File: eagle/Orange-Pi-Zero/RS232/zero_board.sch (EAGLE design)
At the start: 17 parts, among them J1 RS-232, U1 MAX3232CDR

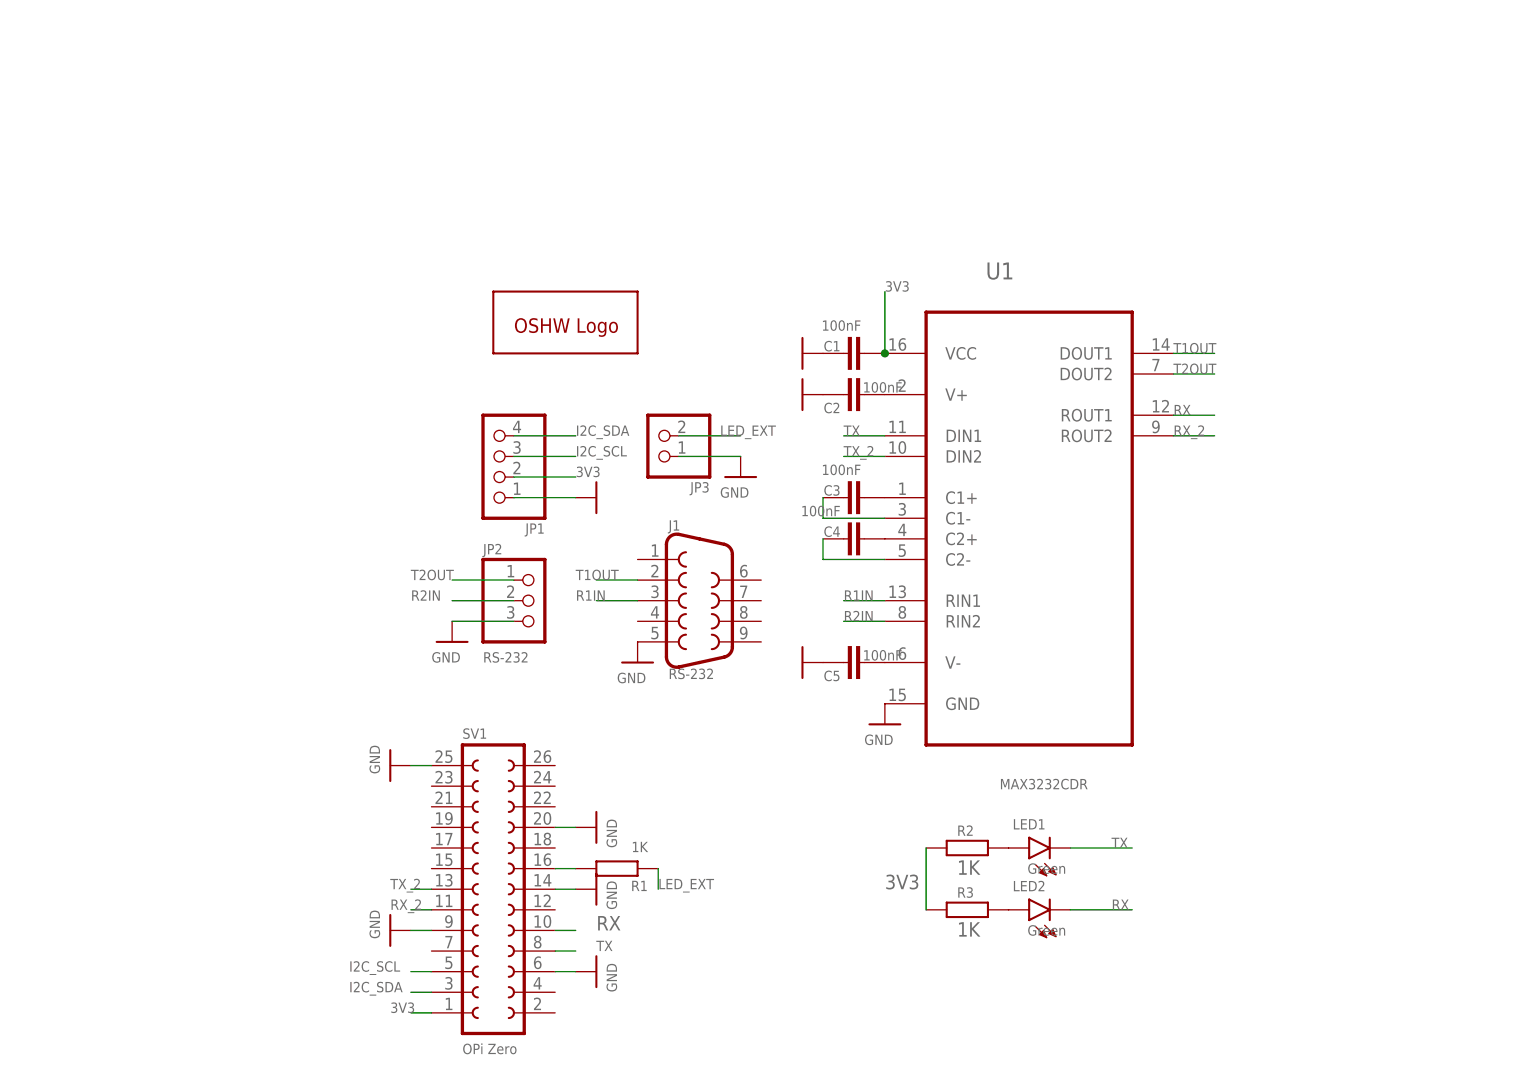
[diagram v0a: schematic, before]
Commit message: Added RGB Panel board.
*. Updated RS232 board
*. Minor fix in BOM fort the 8x pixel board
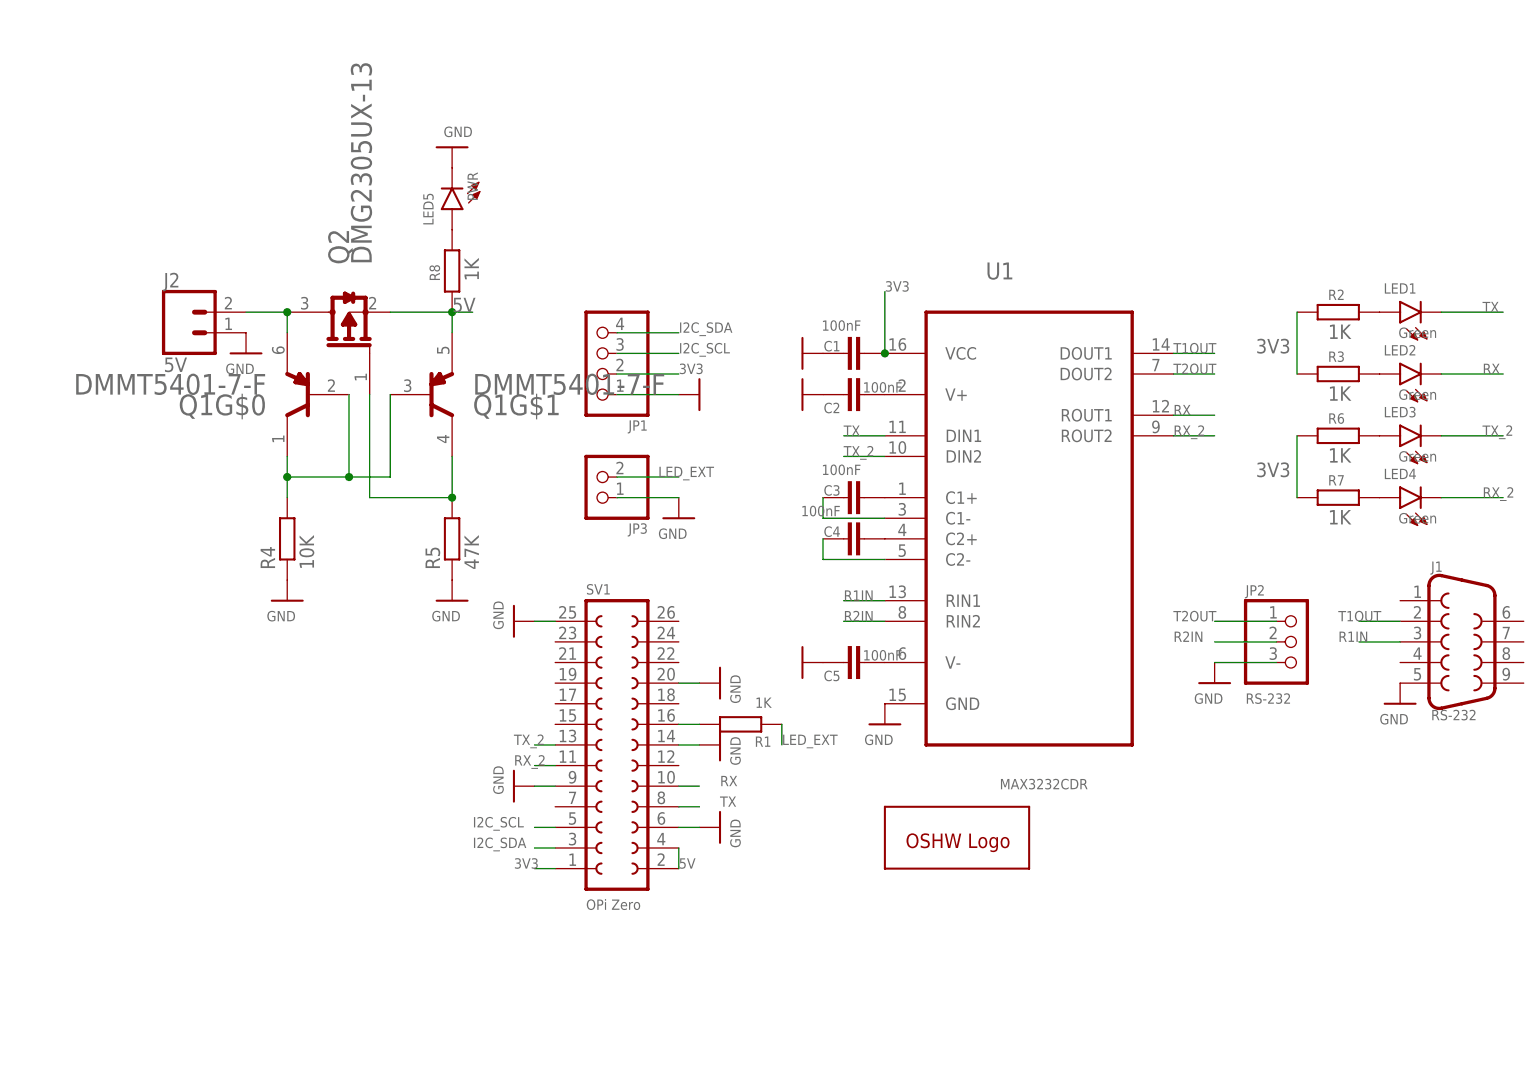
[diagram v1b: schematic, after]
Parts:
- added J2: 5V, SparkFun-Connectors:CONN_023.5MM
- added LED3, LED4: Green, led:LEDCHIP-LED0603
- added LED5: PWR, led:LEDCHIP-LED0603
- added Q1: DIODES_DMMT5401-7-FDIODES_DMMT5401-7-F_0_0, Diodes - DMMT5401-7-F:DIODES_DMMT5401-7-FDIODES_DMMT5401-7-F_0_0
- added Q2: DIODES_INC._DMG2305UX-13DIODES_INC._DMG2305UX-13_0_0, Diodes Inc. - DMG2305UX-13:DIODES_INC._DMG2305UX-13DIODES_INC._DMG2305UX-13_0_0
- added R4: 10K, rcl:R-EU_R0402
- added R5: 47K, rcl:R-EU_R0402
- added R6, R7, R8: 1K, resistor:R-EU_R0603
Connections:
- new net 5V: Q1G$1.E2, Q2.S, R8.1, SV1.2, SV1.4
- new net N$10: Q1G$0.B1, Q1G$0.C1, Q1G$1.B2, R4.2
- new net N$11: J2.2, Q1G$0.E1, Q2.D
- new net N$12: Q1G$1.C2, Q2.G, R5.2
- new net N$13: LED3.A, R6.2
- new net N$14: LED4.A, R7.2
- new net N$15: LED5.A, R8.2
- net 3V3: now also R6.1, R7.1
- net GND: now also J2.1, LED5.C, R4.1, R5.1
- net RX_2: now also LED4.C
- net TX_2: now also LED3.C
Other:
- moved on the sheet: J1, JP1, JP2, JP3, LED1, LED2, R1, R2, R3, SV1
